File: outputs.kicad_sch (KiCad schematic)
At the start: 36 parts, among them J4 PH-2P, J5 PH-2P, J6 PH-3P, J7 MF3-2P, J8 PH-3P, J9 XH-4P, Q1 AON7804, Q2 AON7524, U5 74LVC2G17, U6 TMC2209-LA

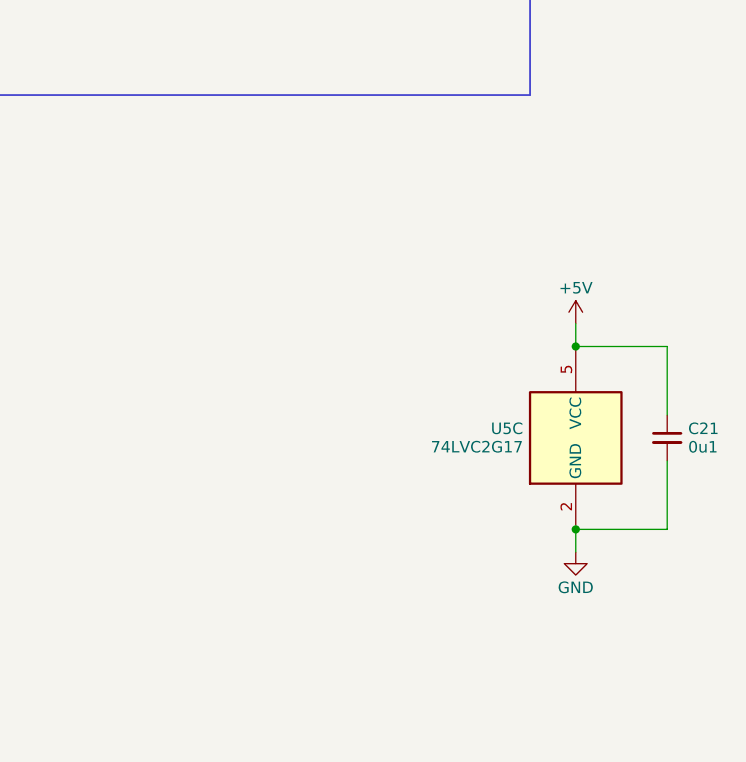
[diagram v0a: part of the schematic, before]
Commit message: Added solder jumpers for CAN/USB interface selection
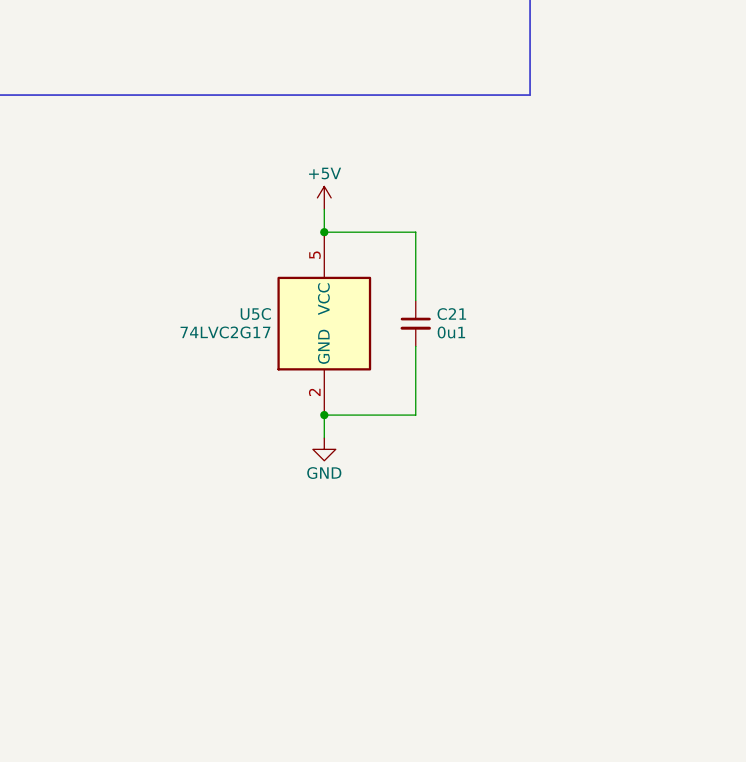
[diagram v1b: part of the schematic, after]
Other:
- moved on the sheet: C21, U5C
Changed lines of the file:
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@@
 	)
 	(junction
-		(at 256.54 129.54)
+		(at 228.6 116.84)
 		(diameter 0)
 		(color 0 0 0 0)
@@
 	)
 	(junction
-		(at 256.54 149.86)
+		(at 228.6 137.16)
 		(diameter 0)
 		(color 0 0 0 0)
@@
 	(wire
 		(pts
-			(xy 256.54 152.4) (xy 256.54 149.86)
+			(xy 228.6 139.7) (xy 228.6 137.16)
 		)
 		(stroke
@@
 	(wire
 		(pts
-			(xy 256.54 129.54) (xy 266.7 129.54)
+			(xy 228.6 116.84) (xy 238.76 116.84)
 		)
 		(stroke
@@
 	(wire
 		(pts
-			(xy 266.7 149.86) (xy 256.54 149.86)
+			(xy 238.76 137.16) (xy 228.6 137.16)
 		)
 		(stroke
@@
 	(wire
 		(pts
-			(xy 256.54 127) (xy 256.54 129.54)
+			(xy 228.6 114.3) (xy 228.6 116.84)
 		)
 		(stroke
@@
 	(wire
 		(pts
-			(xy 266.7 129.54) (xy 266.7 137.16)
+			(xy 238.76 116.84) (xy 238.76 124.46)
 		)
 		(stroke
@@
 	(wire
 		(pts
-			(xy 266.7 142.24) (xy 266.7 149.86)
+			(xy 238.76 129.54) (xy 238.76 137.16)
 		)
 		(stroke
@@
 	(symbol
 		(lib_id "power:+5V")
-		(at 256.54 127 0)
+		(at 228.6 114.3 0)
 		(unit 1)
 		(exclude_from_sim no)
@@
 		(fields_autoplaced yes)
 		(property "Reference" "#PWR052"
-			(at 256.54 130.81 0)
+			(at 228.6 118.11 0)
 			(effects
 				(font
@@
 		)
 		(property "Value" "+5V"
-			(at 256.54 123.055 0)
+			(at 228.6 110.355 0)
 			(effects
 				(font
@@
 		)
 		(property "Footprint" ""
-			(at 256.54 127 0)
+			(at 228.6 114.3 0)
 			(effects
 				(font
@@
 		)
 		(property "Datasheet" ""
-			(at 256.54 127 0)
+			(at 228.6 114.3 0)
 			(effects
 				(font
@@
 		)
 		(property "Description" "Power symbol creates a global label with name \"+5V\""
-			(at 256.54 127 0)
+			(at 228.6 114.3 0)
 			(effects
 				(font
@@
 	(symbol
 		(lib_id "Device:C_Small")
-		(at 266.7 139.7 0)
+		(at 238.76 127 0)
 		(unit 1)
 		(exclude_from_sim no)
@@
 		(fields_autoplaced yes)
 		(property "Reference" "C21"
-			(at 269.0241 138.6823 0)
+			(at 241.0841 125.9823 0)
 			(effects
 				(font
@@
 		)
 		(property "Value" "0u1"
-			(at 269.0241 140.7303 0)
+			(at 241.0841 128.0303 0)
 			(effects
 				(font
@@
 		)
 		(property "Footprint" "Capacitor_SMD:C_0402_1005Metric"
-			(at 266.7 139.7 0)
+			(at 238.76 127 0)
 			(effects
 				(font
@@
 		)
 		(property "Datasheet" "~"
-			(at 266.7 139.7 0)
+			(at 238.76 127 0)
 			(effects
 				(font
@@
 		)
 		(property "Description" ""
-			(at 266.7 139.7 0)
+			(at 238.76 127 0)
 			(effects
 				(font
@@
 		)
 		(property "MPN" ""
-			(at 266.7 139.7 0)
+			(at 238.76 127 0)
 			(effects
 				(font
@@
 		)
 		(property "LCSC" "C307331"
-			(at 266.7 139.7 0)
+			(at 238.76 127 0)
 			(effects
 				(font
@@
 	(symbol
 		(lib_id "74xGxx:74LVC2G17")
-		(at 256.54 139.7 0)
+		(at 228.6 127 0)
 		(unit 3)
 		(exclude_from_sim no)
@@
 		(fields_autoplaced yes)
 		(property "Reference" "U5"
-			(at 250.698 138.676 0)
+			(at 222.758 125.976 0)
 			(effects
 				(font
@@
 		)
 		(property "Value" "74LVC2G17"
-			(at 250.698 140.724 0)
+			(at 222.758 128.024 0)
 			(effects
 				(font
@@
 		)
 		(property "Footprint" "Package_TO_SOT_SMD:SOT-363_SC-70-6"
-			(at 256.54 139.7 0)
+			(at 228.6 127 0)
 			(effects
 				(font
@@
 		)
 		(property "Datasheet" "http://www.ti.com/lit/sg/scyt129e/scyt129e.pdf"
-			(at 256.54 139.7 0)
+			(at 228.6 127 0)
 			(effects
 				(font
@@
 		)
 		(property "Description" "Dual Buffer, Schmitt Triggered, Low-Voltage CMOS"
-			(at 256.54 139.7 0)
+			(at 228.6 127 0)
 			(effects
 				(font
@@
 		)
 		(property "MPN" ""
-			(at 256.54 139.7 0)
+			(at 228.6 127 0)
 			(effects
 				(font
@@
 	(symbol
 		(lib_id "power:GND")
-		(at 256.54 152.4 0)
+		(at 228.6 139.7 0)
 		(unit 1)
 		(exclude_from_sim no)
@@
 		(fields_autoplaced yes)
 		(property "Reference" "#PWR053"
-			(at 256.54 158.75 0)
+			(at 228.6 146.05 0)
 			(effects
 				(font
@@
 		)
 		(property "Value" "GND"
-			(at 256.54 156.345 0)
+			(at 228.6 143.645 0)
 			(effects
 				(font
@@
 		)
 		(property "Footprint" ""
-			(at 256.54 152.4 0)
+			(at 228.6 139.7 0)
 			(effects
 				(font
@@
 		)
 		(property "Datasheet" ""
-			(at 256.54 152.4 0)
+			(at 228.6 139.7 0)
 			(effects
 				(font
@@
 		)
 		(property "Description" "Power symbol creates a global label with name \"GND\" , ground"
-			(at 256.54 152.4 0)
+			(at 228.6 139.7 0)
 			(effects
 				(font

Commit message: Rename fan ports to PCF/HEF
Remove USB series resistors

Add USB clamping diodes
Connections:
- net FAN0 renamed PCFAN
- net FAN0_PWR renamed PCFAN_PWR
- net FAN1 renamed HEFAN
- net FAN1_PWR renamed HEFAN_PWR
- net FAN1_SENSE renamed HEFAN_SENSE
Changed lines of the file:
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@@
 		)
 	)
-	(label "FAN0_PWR"
+	(label "PCFAN_PWR"
 		(at 60.96 106.68 0)
 		(fields_autoplaced yes)
@@
 		)
 	)
-	(label "FAN1_PWR"
+	(label "HEFAN_PWR"
 		(at 60.96 154.94 0)
 		(fields_autoplaced yes)
@@
 		)
 	)
-	(global_label "FAN1"
+	(global_label "HEFAN"
 		(shape input)
 		(at 35.56 165.1 180)
@@
 		)
 		(property "Intersheetrefs" "${INTERSHEET_REFS}"
-			(at 27.937 165.1 0)
+			(at 26.5876 165.1 0)
 			(effects
 				(font
@@
 		)
 	)
-	(global_label "FAN1_SENSE"
+	(global_label "HEFAN_SENSE"
 		(shape output)
 		(at 81.28 177.8 0)
@@
 		)
 		(property "Intersheetrefs" "${INTERSHEET_REFS}"
-			(at 95.9181 177.8 0)
+			(at 97.2675 177.8 0)
 			(effects
 				(font
@@
 		)
 	)
-	(global_label "FAN0"
+	(global_label "PCFAN"
 		(shape input)
 		(at 35.56 116.84 180)
@@
 		)
 		(property "Intersheetrefs" "${INTERSHEET_REFS}"
-			(at 27.937 116.84 0)
-			(effects
-				(font
+			(at 26.5271 116.84 0)
+			(effects
+				(font

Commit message: Add 3D models
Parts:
- J7: MPN (none) -> 43650-0200
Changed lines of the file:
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@@
 			)
 		)
-		(property "MPN" ""
+		(property "MPN" "43650-0200"
 			(at 109.22 35.56 0)
 			(effects

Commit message: Lots of little tweaks and simplifications
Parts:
- JP3, JP4: value Jumper_3_Open -> SolderJumper_3_Open; symbol Jumper:Jumper_3_Open -> Jumper:SolderJumper_3_Open
- R10, R14, R9: value 22K -> 100K; LCSC C25768 -> C25741
- U5: LCSC (none) -> C80500
- U6: LCSC (none) -> C465949; MPN (none) -> TMC2209-LA
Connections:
- net GND: no longer U6.25 (NC)
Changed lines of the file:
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@@
 	)
 	(junction
-		(at 187.96 91.44)
-		(diameter 0)
-		(color 0 0 0 0)
-	)
-	(junction
 		(at 73.66 45.72)
 		(diameter 0)
@@
 	(wire
 		(pts
-			(xy 50.8 149.86) (xy 49.53 149.86)
-		)
-		(stroke
-			(width 0)
-			(type default)
-		)
-	)
-	(wire
-		(pts
 			(xy 73.66 109.22) (xy 60.96 109.22)
 		)
@@
 	(wire
 		(pts
+			(xy 187.96 88.9) (xy 187.96 91.44)
+		)
+		(stroke
+			(width 0)
+			(type default)
+		)
+	)
+	(wire
+		(pts
 			(xy 203.2 48.26) (xy 208.28 48.26)
 		)
@@
 	(wire
 		(pts
-			(xy 36.83 101.6) (xy 35.56 101.6)
+			(xy 38.1 101.6) (xy 35.56 101.6)
 		)
 		(stroke
@@
 	(wire
 		(pts
-			(xy 36.83 149.86) (xy 35.56 149.86)
+			(xy 48.26 149.86) (xy 50.8 149.86)
 		)
 		(stroke
@@
 	(wire
 		(pts
-			(xy 228.6 114.3) (xy 228.6 116.84)
+			(xy 38.1 149.86) (xy 35.56 149.86)
 		)
 		(stroke
@@
 	(wire
 		(pts
-			(xy 43.18 165.1) (xy 43.18 167.64)
+			(xy 228.6 114.3) (xy 228.6 116.84)
 		)
 		(stroke
@@
 	(wire
 		(pts
-			(xy 220.98 38.1) (xy 226.06 38.1)
+			(xy 43.18 165.1) (xy 43.18 167.64)
 		)
 		(stroke
@@
 	(wire
 		(pts
-			(xy 53.34 165.1) (xy 50.8 165.1)
+			(xy 220.98 38.1) (xy 226.06 38.1)
 		)
 		(stroke
@@
 	(wire
 		(pts
-			(xy 190.5 91.44) (xy 187.96 91.44)
+			(xy 53.34 165.1) (xy 50.8 165.1)
 		)
 		(stroke
@@
 	(wire
 		(pts
-			(xy 187.96 91.44) (xy 187.96 93.98)
-		)
-		(stroke
-			(width 0)
-			(type default)
-		)
-	)
-	(wire
-		(pts
 			(xy 104.14 38.1) (xy 96.52 38.1)
 		)
@@
 	(wire
 		(pts
-			(xy 187.96 88.9) (xy 187.96 91.44)
-		)
-		(stroke
-			(width 0)
-			(type default)
-		)
-	)
-	(wire
-		(pts
 			(xy 167.64 127) (xy 170.18 127)
 		)
@@
 	(wire
 		(pts
-			(xy 190.5 88.9) (xy 190.5 91.44)
-		)
-		(stroke
-			(width 0)
-			(type default)
-		)
-	)
-	(wire
-		(pts
 			(xy 73.66 109.22) (xy 73.66 119.38)
 		)
@@
 	(wire
 		(pts
-			(xy 50.8 101.6) (xy 49.53 101.6)
+			(xy 50.8 101.6) (xy 48.26 101.6)
 		)
 		(stroke
@@
 			)
 		)
-		(property "Value" "22K"
+		(property "Value" "100K"
 			(at 44.6786 171.204 0)
 			(effects
@@
 			)
 		)
-		(property "LCSC" "C25768"
+		(property "LCSC" "C25741"
 			(at 43.18 170.18 0)
 			(effects
@@
 	(symbol
 		(lib_id "power:GND")
-		(at 187.96 93.98 0)
+		(at 187.96 91.44 0)
 		(unit 1)
 		(exclude_from_sim no)
@@
 		(fields_autoplaced yes)
 		(property "Reference" "#PWR043"
-			(at 187.96 100.33 0)
+			(at 187.96 97.79 0)
 			(effects
 				(font
@@
 		)
 		(property "Value" "GND"
-			(at 187.96 97.925 0)
+			(at 187.96 95.385 0)
 			(effects
 				(font
@@
 		)
 		(property "Footprint" ""
-			(at 187.96 93.98 0)
+			(at 187.96 91.44 0)
 			(effects
 				(font
@@
 		)
 		(property "Datasheet" ""
-			(at 187.96 93.98 0)
+			(at 187.96 91.44 0)
 			(effects
 				(font
@@
 		)
 		(property "Description" "Power symbol creates a global label with name \"GND\" , ground"
-			(at 187.96 93.98 0)
+			(at 187.96 91.44 0)
 			(effects
 				(font
@@
 			)
 		)
+		(property "LCSC" "C80500"
+			(at 58.42 45.72 0)
+			(effects
+				(font
+					(size 1.27 1.27)
+				)
+				(hide yes)
+			)
+		)
 		(pin "1"
 		)
@@
 			)
 		)
-		(property "Value" "22K"
+		(property "Value" "100K"
 			(at 44.6786 122.944 0)
 			(effects
@@
 			)
 		)
-		(property "LCSC" "C25768"
+		(property "LCSC" "C25741"
 			(at 43.18 121.92 0)
 			(effects
@@
 			)
 		)
+		(property "LCSC" "C80500"
+			(at 228.6 127 0)
+			(effects
+				(font
+					(size 1.27 1.27)
+				)
+				(hide yes)
+			)
+		)
 		(pin "1"
 		)
@@
 	)
 	(symbol
-		(lib_id "Jumper:Jumper_3_Open")
+		(lib_id "Jumper:SolderJumper_3_Open")
 		(at 43.18 101.6 0)
 		(unit 1)
@@
 			)
 		)
-		(property "Value" "Jumper_3_Open"
+		(property "Value" "SolderJumper_3_Open"
 			(at 43.18 98.6958 0)
 			(effects
@@
 			)
 		)
-		(property "Description" ""
+		(property "Description" "Solder Jumper, 3-pole, open"
 			(at 43.18 101.6 0)
 			(effects
@@
 			)
 		)
-		(property "Value" "22K"
+		(property "Value" "100K"
 			(at 80.2386 51.824 0)
 			(effects
@@
 			)
 		)
-		(property "LCSC" "C25768"
+		(property "LCSC" "C25741"
 			(at 78.74 50.8 0)
 			(effects
@@
 	)
 	(symbol
-		(lib_id "Jumper:Jumper_3_Open")
+		(lib_id "Jumper:SolderJumper_3_Open")
 		(at 43.18 149.86 0)
 		(unit 1)
@@
 			)
 		)
-		(property "Value" "Jumper_3_Open"
+		(property "Value" "SolderJumper_3_Open"
 			(at 43.18 146.9558 0)
 			(effects
@@
 			)
 		)
-		(property "Description" ""
+		(property "Description" "Solder Jumper, 3-pole, open"
 			(at 43.18 149.86 0)
 			(effects
@@
 		(fields_autoplaced yes)
 		(property "Reference" "U6"
-			(at 192.4559 87.892 0)
+			(at 190.1541 88.0801 0)
 			(effects
 				(font
@@
 		)
 		(property "Value" "TMC2209-LA"
-			(at 192.4559 89.94 0)
+			(at 190.1541 90.5044 0)
 			(effects
 				(font
@@
 			)
 		)
-		(property "MPN" ""
+		(property "MPN" "TMC2209-LA"
+			(at 187.96 63.5 0)
+			(effects
+				(font
+					(size 1.27 1.27)
+				)
+				(hide yes)
+			)
+		)
+		(property "LCSC" "C465949"
 			(at 187.96 63.5 0)
 			(effects
@@
 			(at 142.24 129.54 0)
 			(effects
+				(font
+					(size 1.27 1.27)
+				)
+				(hide yes)
+			)
+		)
+		(property "LCSC" "C80500"
+			(at 142.24 129.54 0)
+			(effects

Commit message: Add part number references
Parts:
- C13, C14, C15: manf# (none) -> CL10A475KO8NNNC
- C16, C17, C18, C19, C20, C21: manf# (none) -> GRM155R71H104KE14J
- D3: manf# (none) -> LTST-S270KRKT
- D4: digikey# (none) -> 1655-DSS14UCT-ND; manf# (none) -> DSS14
- J4, J5: manf# (none) -> B2B-PH-K-S
- J6, J8: manf# (none) -> B3B-PH-K-S
- J7: manf# (none) -> 43650-0200
- J9: manf# (none) -> B4B-XH-A
- JP3, JP4: now left out of the parts list
- Q1: manf# (none) -> AON7804
- Q2: manf# (none) -> AON7524
- R10, R14, R9: manf# (none) -> RMCF0402JT100K
- R11, R12, R15: manf# (none) -> RMCF0402JT10R0
- R13: manf# (none) -> RMCF0402JT1K00
- R16, R8: manf# (none) -> RMCF0402FT10K0
- R17: manf# (none) -> RMCF0402FT100R
- R18, R19: manf# (none) -> ERJ-6DSFR11V
- U5: manf# (none) -> SN74LVC2G17DCKR
- U6: manf# (none) -> TMC2209-LA

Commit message: Change input caps
- 100uF to electrolytic
- 10uF to 1206/50V
- Also fix LED on BOM to not be right angle lol
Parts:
- D3: manf# LTST-S270KRKT -> LTST-C190KRKT
- D4: MPN DSS14 -> (none)
- J7: MPN 43650-0200 -> (none)
- Q1: MPN AON7804 -> (none)
- Q2: MPN AON7524 -> (none)
- R18, R19: value 0R11 -> 0R11 1/3W; MPN RL1220S-R11-F -> (none)
- U6: MPN TMC2209-LA -> (none)
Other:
- moved on the sheet: C17, J9, R18, R19

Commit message: Change 5V out cap to 0805
- Shifted power/CAN connector a bit to make room, and added a bit of
  meat to the board around the mounting hole
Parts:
- D4: mouser# (none) -> 241-SS1040FLR100001
- JP3, JP4: now not fitted
- R10, R14, R9: manf# RMCF0402JT100K -> RC0402FR-07100KL
- R11, R12, R15: manf# RMCF0402JT10R0 -> RC0402FR-0710RL
- R13: manf# RMCF0402JT1K00 -> RC0402FR-071KL
- R16, R8: manf# RMCF0402FT10K0 -> RC0402FR-0710KL
- R17: manf# RMCF0402FT100R -> RC0402FR-07100RL

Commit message: Update LCSC part numbers
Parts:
- J7: LCSC C114089 -> C192562
- U5: LCSC C80500 -> C7394037
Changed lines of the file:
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@@
 			)
 		)
-		(property "LCSC" "C80500"
+		(property "LCSC" "C7394037"
 			(at 58.42 45.72 0)
 			(effects
@@
 			)
 		)
-		(property "LCSC" "C80500"
+		(property "LCSC" "C7394037"
 			(at 228.6 127 0)
 			(effects
@@
 			)
 		)
-		(property "LCSC" "C114089"
+		(property "LCSC" "C192562"
 			(at 109.22 35.56 0)
 			(effects
@@
 			)
 		)
-		(property "LCSC" "C80500"
+		(property "LCSC" "C7394037"
 			(at 142.24 129.54 0)
 			(effects
